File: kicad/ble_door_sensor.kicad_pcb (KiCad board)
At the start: 4 copper layers, 20 x 60 mm, 43 parts, among them J1 Prog Header, J2 Prog Header, P10 TestPoint, P12 TestPoint, P14 TestPoint, P19 TestPoint, P20 TestPoint, P27 TestPoint, P29 TestPoint, P3 TestPoint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

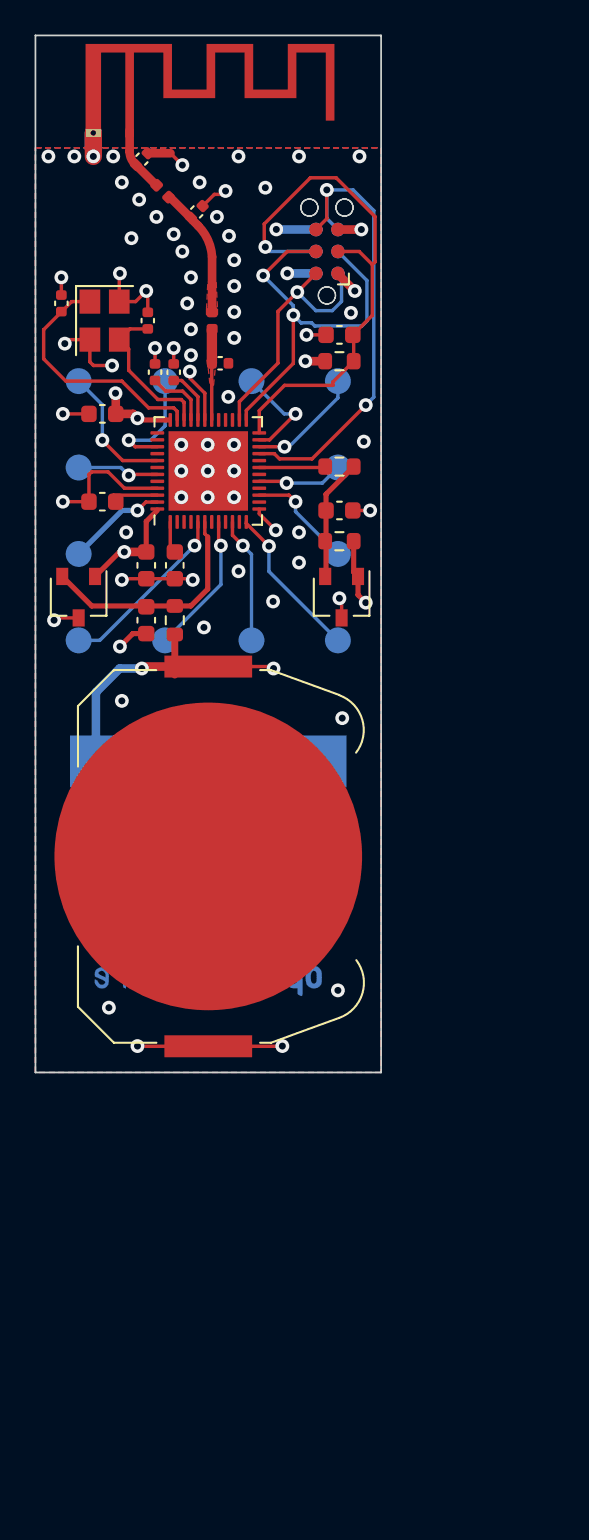
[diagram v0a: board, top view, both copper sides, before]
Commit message: First rough placement
Updated some footprints in the process to better fit my needs

Holes are in 5mm grid to each other 15mm in x and 45 mm in y apart

Board outline is 20x80mm
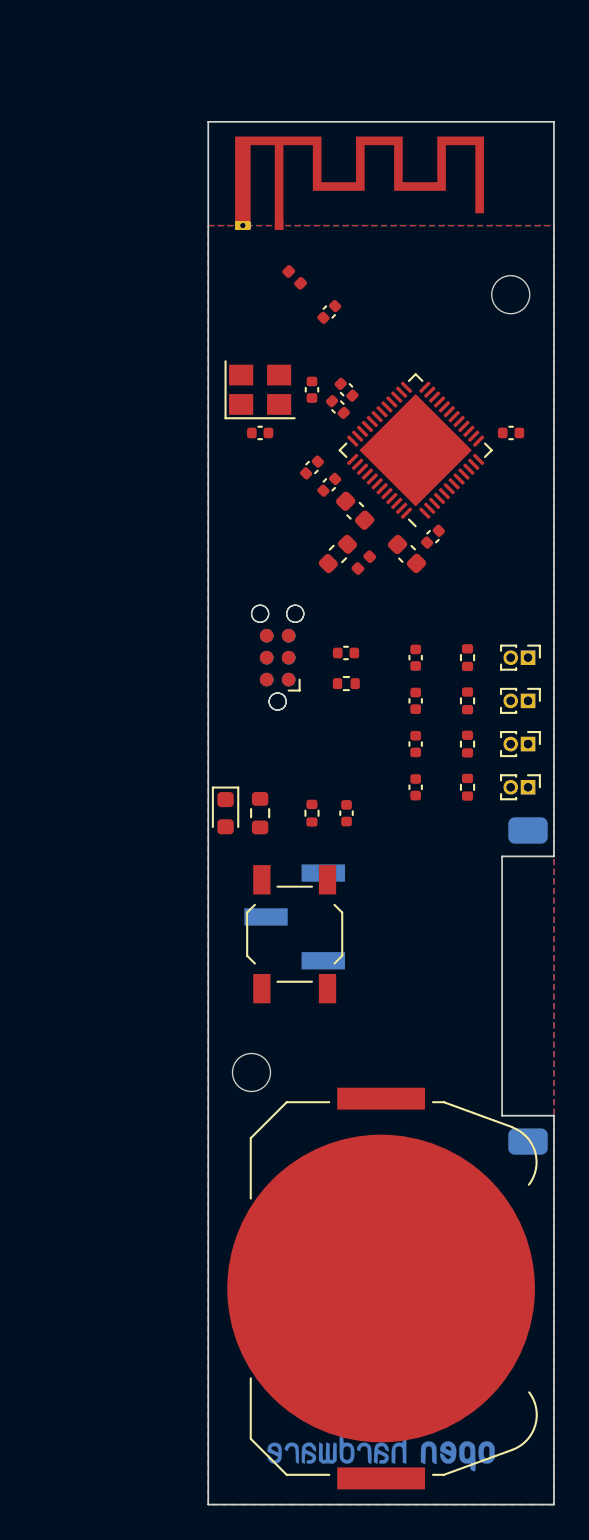
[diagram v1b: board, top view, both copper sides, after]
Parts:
- removed C10, C12: C_Small, Capacitor_SMD:C_0402_1005Metric
- removed C14: 100nF, Capacitor_SMD:C_0603_1608Metric
- removed DCC1, P10, P12, P14, P19, P20, P27, P29, P3, P31, P6, P8: TestPoint, TestPoint:TestPoint_Pad_D1.5mm
- removed L2: L, Inductor_SMD:L_0402_1005Metric
- removed R3: 0R, Resistor_SMD:R_0603_1608Metric
- removed R4: 470k, Resistor_SMD:R_0603_1608Metric
- removed U2, U3: A3214ELHLT-T, Package_TO_SOT_SMD:SOT-23W
- added C101: 100nF, Capacitor_SMD:C_0402_1005Metric, F.Cu at (133.0, 80.0)
- added C102: 100nF, Capacitor_SMD:C_0402_1005Metric, F.Cu at (137.0, 76.0)
- added C103: 100nF, Capacitor_SMD:C_0402_1005Metric, F.Cu at (137.0, 73.5)
- added C104: 100nF, Capacitor_SMD:C_0402_1005Metric, F.Cu at (137.0, 71.0)
- added C105: 12pF, Capacitor_SMD:C_0402_1005Metric, F.Cu at (132.0, 61.0)
- added C106: 12pF, Capacitor_SMD:C_0402_1005Metric, F.Cu at (131.0, 60.0)
- added D101: LED, LED_SMD:LED_0603_1608Metric, F.Cu at (126.0, 80.0)
- added H101: MountingHole, MountingHole:MountingHole_2.2mm_M2, F.Cu at (127.5, 95.0)
- added H102: MountingHole, MountingHole:MountingHole_2.2mm_M2, F.Cu at (142.5, 50.0)
- added J101: Conn_01x03_Pin, Connector_PinHeader_2.54mm:PinHeader_1x03_P2.54mm_Vertical_SMD_Pin1Left, B.Cu at (130.0, 86.0)
- added L101: 15nH, Inductor_SMD:L_0402_1005Metric, F.Cu at (134.0, 65.5)
- added L102: 10uH, Inductor_SMD:L_0603_1608Metric, F.Cu at (132.5, 65.0)
- added R101: 100k, Resistor_SMD:R_0402_1005Metric, F.Cu at (131.0, 80.0)
- added R102: 1K, Resistor_SMD:R_0603_1608Metric, F.Cu at (128.0, 80.0)
- added R103: 470k, Resistor_SMD:R_0402_1005Metric, F.Cu at (140.0, 76.0)
- added R104: 470k, Resistor_SMD:R_0402_1005Metric, F.Cu at (140.0, 73.5)
- added R105: 470k, Resistor_SMD:R_0402_1005Metric, F.Cu at (140.0, 71.0)
- added SW101: SW_Reed, Library:reed_contact, B.Cu at (143.5, 90.0)
- added SW102: SW_Push, Button_Switch_SMD:SW_SPST_TL3342, F.Cu at (130.0, 87.0)
- added SW103: REED_EXT, Connector_PinHeader_1.00mm:PinHeader_1x02_P1.00mm_Vertical, F.Cu at (143.5, 76.0)
- added SW104: REED_EXT, Connector_PinHeader_1.00mm:PinHeader_1x02_P1.00mm_Vertical, F.Cu at (143.5, 73.5)
- added SW105: REED_EXT, Connector_PinHeader_1.00mm:PinHeader_1x02_P1.00mm_Vertical, F.Cu at (143.5, 71.0)
- added SW106: REED_EXT, Connector_PinHeader_1.00mm:PinHeader_1x02_P1.00mm_Vertical, F.Cu at (143.5, 78.5)
- C1, C11, C13, C3: footprint Capacitor_SMD:C_0603_1608Metric -> Capacitor_SMD:C_0402_1005Metric
- L1: value 3.3nF -> 3.3nH
- R1, R2: footprint Resistor_SMD:R_0603_1608Metric -> Resistor_SMD:R_0402_1005Metric
- moved TP1 29.3 mm to (130.0, 104.0)
- moved REF** 29.3 mm to (135.0, 112.5)
- moved TP2 28.3 mm to (140.0, 104.0)
- moved BT1 26.9 mm to (135.0, 107.5)
- moved C1 23.7 mm to (142.5, 58.0), turned to 0 degrees
- moved J1 23.7 mm to (129.0, 71.0)
- moved J2 23.7 mm to (129.0, 71.0)
- moved R1 18.7 mm to (133.0, 72.5)
- moved C3 18.4 mm to (133.0, 70.7)
- moved C13 16.6 mm to (137.0, 78.5), turned to -90 degrees
- moved R2 16.1 mm to (140.0, 78.5), turned to 90 degrees
- moved C2 15.1 mm to (136.5, 65.0), turned to -45 degrees
- moved C11 15.0 mm to (138.0, 64.0), turned to -135 degrees
- moved C5 14.6 mm to (133.5, 62.5), turned to 135 degrees
- moved C6 13.7 mm to (128.0, 58.0), turned to 0 degrees
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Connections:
- C13 pad 1: Net-(U2-VOUT) -> ONBOARD_HALL
- L1 pad 2: Net-(C10-Pad1) -> Net-(AE1-A)
- R2 pad 2: Net-(U2-VOUT) -> ONBOARD_HALL
- U1 pad 10: Net-(U1-P0.08) -> unconnected-(U1-P0.08-Pad10)
- U1 pad 12: Net-(U1-NFC2/P0.10) -> unconnected-(U1-NFC2/P0.10-Pad12)
- U1 pad 14: unconnected-(U1-P0.11-Pad14) -> ONBOARD_HALL
- U1 pad 15: Net-(U1-P0.12) -> unconnected-(U1-P0.12-Pad15)
- U1 pad 17: Net-(U1-P0.14) -> unconnected-(U1-P0.14-Pad17)
- U1 pad 19: ONBOARD_HALL -> unconnected-(U1-P0.16-Pad19)
- U1 pad 22: Net-(U1-P0.19) -> unconnected-(U1-P0.19-Pad22)
- U1 pad 23: Net-(U1-P0.20) -> unconnected-(U1-P0.20-Pad23)
- U1 pad 37: unconnected-(U1-P0.25-Pad37) -> Net-(U1-P0.25)
- U1 pad 38: unconnected-(U1-P0.26-Pad38) -> Net-(U1-P0.26)
- U1 pad 39: Net-(U1-P0.27) -> unconnected-(U1-P0.27-Pad39)
- U1 pad 41: Net-(U1-P0.29/AIN5) -> unconnected-(U1-P0.29/AIN5-Pad41)
- U1 pad 43: Net-(U1-P0.31/AIN7) -> unconnected-(U1-P0.31/AIN7-Pad43)
- U1 pad 5: Net-(U1-P0.03/AIN1) -> unconnected-(U1-P0.03/AIN1-Pad5)
- U1 pad 6: ONBOARD_HALL_2 -> unconnected-(U1-P0.04/AIN2-Pad6)
- U1 pad 8: Net-(U1-P0.06) -> unconnected-(U1-P0.06-Pad8)
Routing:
- net VCC: track 46.3 -> 0.00 mm, vias 12 -> 0
- net GND: track 44.6 -> 0.00 mm, vias 68 -> 0
- net RESET: track 32.1 -> 0.00 mm, vias 1 -> 0
- net SWO: track 27.3 -> 0.00 mm, vias 2 -> 0
- net SWCLK: track 23.2 -> 0.00 mm, vias 2 -> 0
- net SWDIO: track 15.2 -> 0.00 mm, vias 1 -> 0
- net Net-(U1-XC2): track 14.5 -> 0.00 mm
- net ONBOARD_HALL_2: track 13.5 -> 0.00 mm
- net Net-(U1-P0.03/AIN1): track 10.4 -> 0.00 mm, vias 1 -> 0
- net Net-(U1-NFC2/P0.10): track 9.05 -> 0.00 mm, vias 1 -> 0
- net Net-(U1-XC1): track 8.90 -> 0.00 mm
- net Net-(U1-P0.06): track 8.24 -> 0.00 mm, vias 1 -> 0
- net Net-(U1-P0.29/AIN5): track 7.65 -> 0.00 mm, vias 1 -> 0
- net Net-(U1-P0.08): track 7.31 -> 0.00 mm, vias 1 -> 0
- net Net-(C10-Pad1): track 7.08 -> 0.00 mm
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- removed copper zone on F.Cu, net ANTENNA
- removed copper zone on F.Cu, net Net-(C10-Pad1)
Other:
- board size 20 x 60 mm -> 20 x 80 mm
- board text added: "EXT 1"
- board text added: "EXT 2"
- board text added: "EXT 3"
- board text added: "INT"
- board text added: "RX"
- board text added: "TX"
- board text added: "v0.2"
- board text removed: "DCC"
- board text removed: "v0.1"

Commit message: First routing
Replaced Testpoints with SMD pinheader
Added more Testpoints
Reduced board outline to 20x70mm
Mounting holes are now 15x35mm apart
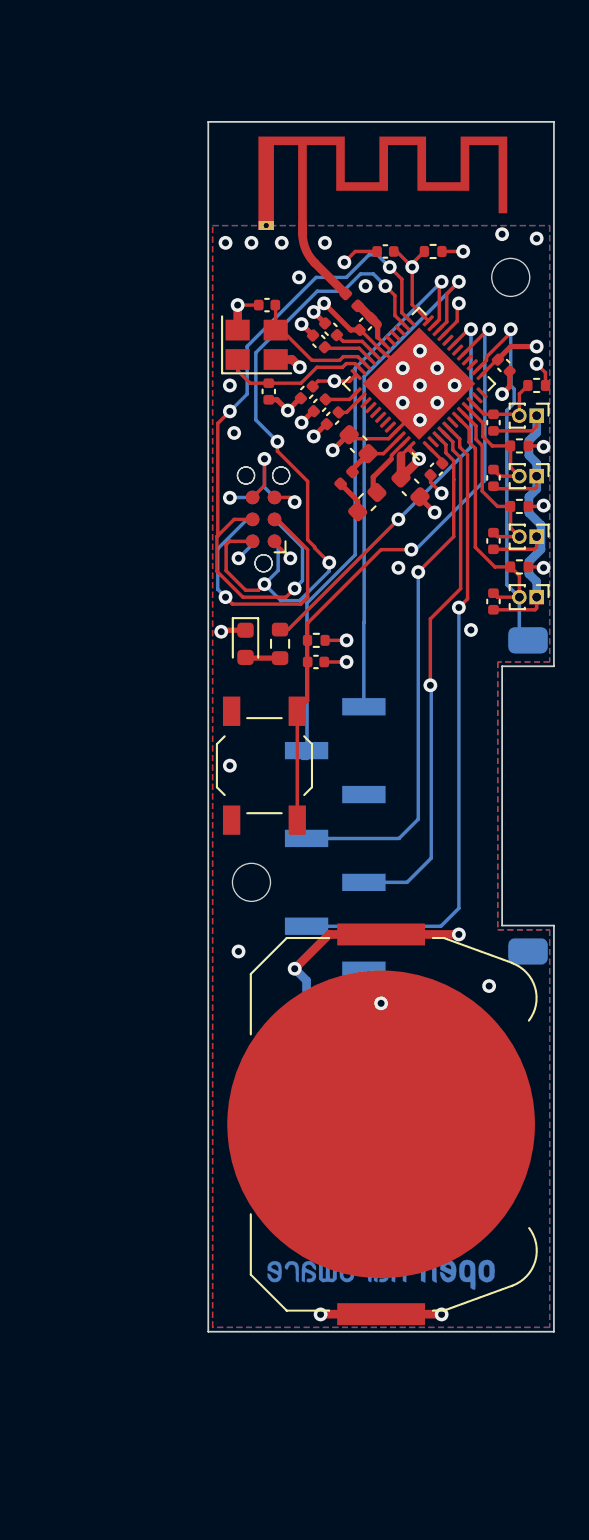
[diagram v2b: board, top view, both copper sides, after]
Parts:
- removed TP1, TP2: TestPoint, TestPoint:TestPoint_Pad_3.0x3.0mm
- added C107: 100nF, Capacitor_SMD:C_0402_1005Metric, F.Cu at (130.7, 55.6)
- J101: value Conn_01x03_Pin -> Conn_01x08; footprint Connector_PinHeader_2.54mm:PinHeader_1x03_P2.54mm_Vertical_SMD_Pin1Left -> Connector_PinHeader_2.54mm:PinHeader_1x08_P2.54mm_Vertical_SMD_Pin1Left
- moved R1 25.5 mm to (138.0, 47.5), turned to 180 degrees
- moved C3 23.3 mm to (135.2, 47.5)
- moved R105 16.3 mm to (144.0, 55.2), turned to 180 degrees
- moved R104 15.1 mm to (143.0, 58.8), turned to 180 degrees
- moved C104 14.3 mm to (141.5, 57.4)
- moved R103 14.1 mm to (143.0, 62.2), turned to 180 degrees
- moved SW105 14.0 mm to (144.0, 57.0)
- moved C103 13.7 mm to (141.5, 60.6)
- moved R2 13.1 mm to (143.0, 65.8), turned to 180 degrees
- moved SW104 13.0 mm to (144.0, 60.5)
- moved C102 12.6 mm to (141.5, 64.2)
- moved SW103 12.0 mm to (144.0, 64.0)
- moved C13 11.7 mm to (141.5, 67.8)
- moved SW106 11.0 mm to (144.0, 67.5)
- moved H101 11.0 mm to (127.5, 84.0)
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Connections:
- L101 pad 1: Net-(L101-Pad1) -> Net-(U1-DEC4)
- L101 pad 2: Net-(U1-DCC) -> Net-(L101-Pad2)
- L102 pad 1: Net-(U1-DEC4) -> Net-(L101-Pad2)
- L102 pad 2: Net-(L101-Pad1) -> Net-(U1-DCC)
- U1 pad 10: unconnected-(U1-P0.08-Pad10) -> EXT_HALL_3
- U1 pad 17: unconnected-(U1-P0.14-Pad17) -> BUTTON
- U1 pad 19: unconnected-(U1-P0.16-Pad19) -> LED
- U1 pad 22: unconnected-(U1-P0.19-Pad22) -> RX
- U1 pad 23: unconnected-(U1-P0.20-Pad23) -> TX
- U1 pad 3: unconnected-(U1-P0.01/XL2-Pad3) -> P0.01
- U1 pad 4: unconnected-(U1-P0.02/AIN0-Pad4) -> P0.02
- U1 pad 5: unconnected-(U1-P0.03/AIN1-Pad5) -> P0.03
- U1 pad 7: unconnected-(U1-P0.05/AIN3-Pad7) -> ONBOARD_HALL
- U1 pad 8: unconnected-(U1-P0.06-Pad8) -> EXT_HALL_1
- U1 pad 9: unconnected-(U1-P0.07-Pad9) -> EXT_HALL_2
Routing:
- net GND: track 0.00 -> 73.1 mm, vias 0 -> 42
- net RESET: track 0.00 -> 49.3 mm, vias 0 -> 2
- net VCC: track 0.00 -> 40.9 mm, vias 0 -> 15
- net SWCLK: track 0.00 -> 40.7 mm, vias 0 -> 3
- net SWDIO: track 0.00 -> 40.5 mm, vias 0 -> 4
- net P0.03: track 0.00 -> 37.8 mm, vias 0 -> 1
- net BUTTON: track 0.00 -> 36.3 mm, vias 0 -> 2
- net ONBOARD_HALL: track 0.00 -> 35.9 mm, vias 0 -> 1
- net TX: track 0.00 -> 34.1 mm, vias 0 -> 1
- net P0.02: track 0.00 -> 30.7 mm, vias 0 -> 1
- net P0.01: track 0.00 -> 30.3 mm, vias 0 -> 1
- net RX: track 0.00 -> 30.2 mm, vias 0 -> 1
- net SWO: track 0.00 -> 24.7 mm, vias 0 -> 2
- net LED: track 0.00 -> 23.7 mm, vias 0 -> 2
- net EXT_HALL_1: track 0.00 -> 10.6 mm
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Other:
- board size 20 x 80 mm -> 20 x 70 mm
- board text added: "Door Monitor v0.2"
- board text added: "Fabian Pflug"
- board text added: "P0.01"
- board text added: "P0.02"
- board text added: "P0.03"
- board text removed: "Door Monitor"
- board text removed: "v0.2"

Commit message: Put the reed contact on the top side
I want to glue the PCB to some surfaces and having something on the
bottom side is very contraproductive.
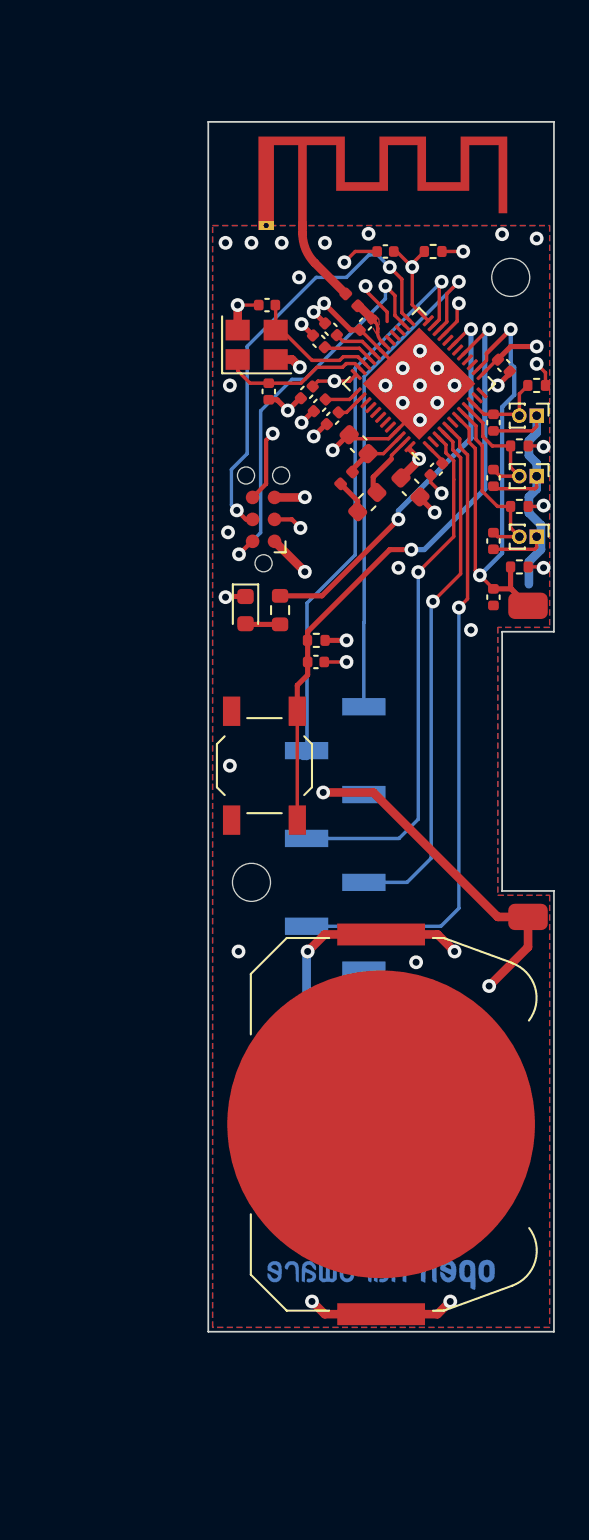
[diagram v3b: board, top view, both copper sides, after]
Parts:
- removed J2: Prog Header, Connector:Tag-Connect_TC2030-IDC-NL_2x03_P1.27mm_Vertical
- removed SW106: REED_EXT, Connector_PinHeader_1.00mm:PinHeader_1x02_P1.00mm_Vertical
- C102, C103, C104, C13: value 100nF -> 10nF
- R103, R104, R105, R2: value 470k -> 1M
- SW101: moved to F.Cu
- moved SW101 2.00 mm to (143.5, 77.0)
- moved D101 1.95 mm to (127.2, 68.2)
- moved R102 1.95 mm to (129.2, 68.2)
- moved C13 0.25 mm to (141.5, 67.5)
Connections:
- SW101 pad 1: GND -> ONBOARD_HALL
- SW101 pad 2: ONBOARD_HALL -> GND
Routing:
- net RESET: track 49.3 -> 30.9 mm
- net SWDIO: track 40.5 -> 23.3 mm, vias 4 -> 2
- net GND: track 73.1 -> 88.6 mm, vias 42 -> 43
- net SWCLK: track 40.7 -> 25.4 mm, vias 3 -> 2
- net SWO: track 24.7 -> 22.3 mm
- net ONBOARD_HALL: track 35.9 -> 34.1 mm, vias 1 -> 2
- net VCC: track 40.9 -> 40.0 mm, vias 15 -> 14
- net LED: track 23.7 -> 22.9 mm
- added copper zone on F.Cu, net ANTENNA
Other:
- outline, holes or cut-outs redrawn
- board text removed: "INT"

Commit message: Add Temperature sensor instead of external reed
Remove the contacts fro external reed contacts
Add temperature sensor
Reduce the size of the PCB
Add additional mounting hole
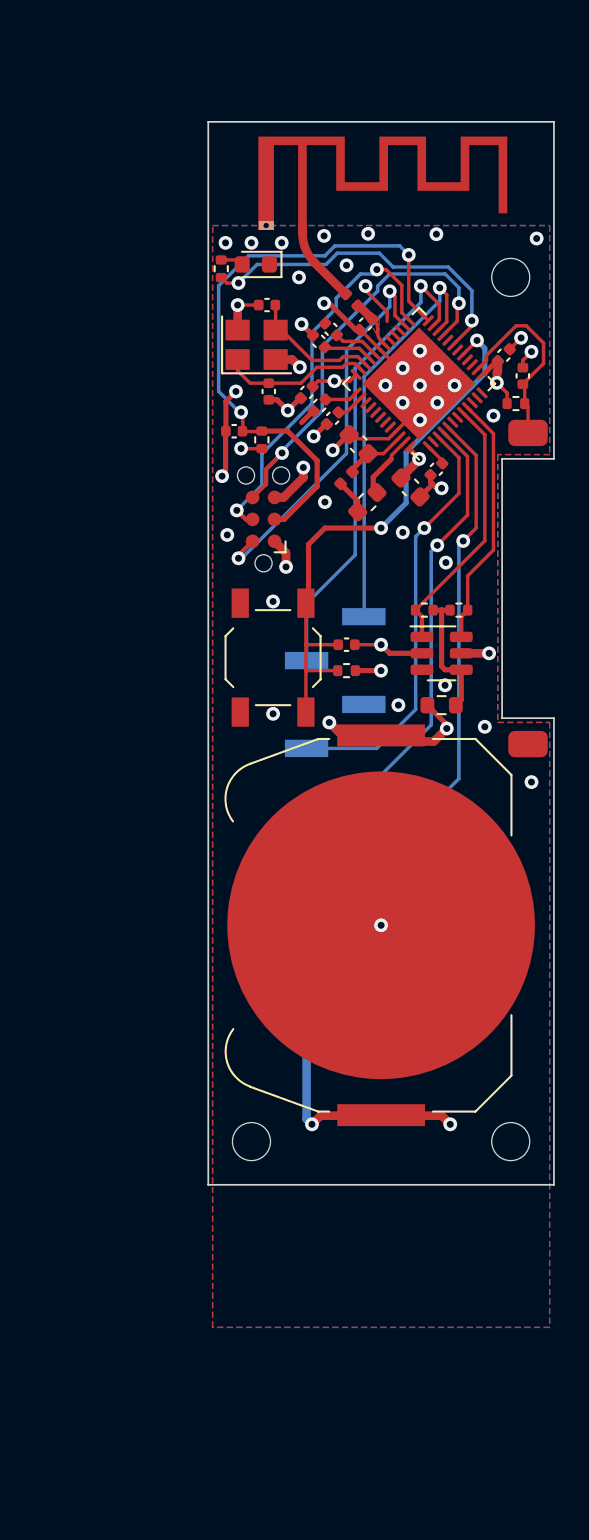
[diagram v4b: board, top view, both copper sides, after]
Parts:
- removed C102, C103, C104: 10nF, Capacitor_SMD:C_0402_1005Metric
- removed REF**: OSHW-Logo2_14.6x12mm_Copper, Symbol:OSHW-Logo2_14.6x12mm_Copper
- removed SW103, SW104, SW105: REED_EXT, Connector_PinHeader_1.00mm:PinHeader_1x02_P1.00mm_Vertical
- added H103: MountingHole, MountingHole:MountingHole_2.2mm_M2, F.Cu at (142.5, 99.0)
- added U101: TMP100, Package_TO_SOT_SMD:SOT-23-6, F.Cu at (138.5, 70.8)
- R102: footprint Resistor_SMD:R_0603_1608Metric -> Resistor_SMD:R_0402_1005Metric
- R103: value 1M -> 0; footprint Resistor_SMD:R_0402_1005Metric -> Resistor_SMD:R_0603_1608Metric
- R104, R105: value 1M -> 100k
- moved R102 20.0 mm to (125.8, 48.5), turned to 90 degrees
- moved D101 20.0 mm to (127.8, 48.2), turned to 180 degrees
- moved H101 15.0 mm to (127.5, 99.0)
- moved R1 14.7 mm to (128.1, 58.4), turned to 90 degrees
- moved R105 14.5 mm to (137.5, 68.2)
- moved C3 13.6 mm to (126.5, 57.9)
- moved C13 12.9 mm to (143.2, 54.7), turned to 90 degrees
- moved R103 12.3 mm to (138.5, 73.8), turned to 0 degrees
- moved BT1 11.5 mm to (135.0, 86.5), turned to -90 degrees
- moved R104 10.1 mm to (139.5, 68.2), turned to 0 degrees
- moved SW101 10.0 mm to (143.5, 67.0)
- moved R2 9.45 mm to (142.8, 56.3), turned to 0 degrees
- moved SW102 6.27 mm to (128.8, 71.0)
- moved J101 5.21 mm to (132.3, 77.5)
- moved R101 2.47 mm to (133.0, 71.8)
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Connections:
- net EXT_HALL_2 renamed SDA
- net Net-(AE1-A) renamed /Antenne
- net Net-(U1-DEC1) renamed /DEC1
- net Net-(U1-DEC2) renamed /DEC2
- net Net-(U1-DEC3) renamed /DEC3
- net Net-(U1-DEC4) renamed /DEC4
- net Net-(U1-XC1) renamed /XC1
- net Net-(U1-XC2) renamed /XC2
- R103 pad 2: EXT_HALL_1 -> /VCC_Temp
- R104 pad 1: VCC -> /VCC_Temp
- R105 pad 1: VCC -> /VCC_Temp
- R105 pad 2: EXT_HALL_3 -> SCL
- U1 pad 10: EXT_HALL_3 -> unconnected-(U1-P0.08-Pad10)
- U1 pad 7: ONBOARD_HALL -> unconnected-(U1-P0.05/AIN3-Pad7)
- U1 pad 8: EXT_HALL_1 -> SCL
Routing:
- net ONBOARD_HALL: track 34.1 -> 11.3 mm, vias 2 -> 0
- net GND: track 88.6 -> 66.2 mm, vias 43 -> 46
- net SCL: track 0.00 -> 15.3 mm
- net EXT_HALL_1: track 10.6 -> 0.00 mm
- net /VCC_Temp: track 0.00 -> 7.63 mm
- net SDA: track 7.49 -> 14.7 mm
- net TX: track 34.1 -> 27.3 mm
- net RX: track 30.2 -> 23.7 mm
- net P0.02: track 30.7 -> 24.4 mm
- net P0.03: track 37.8 -> 31.6 mm
- net P0.01: track 30.3 -> 24.6 mm
- net EXT_HALL_3: track 4.99 -> 0.00 mm
- net RESET: track 30.9 -> 35.3 mm
- net BUTTON: track 36.3 -> 32.8 mm
- net VCC: track 40.0 -> 43.2 mm, vias 14 -> 10
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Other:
- board size 20 x 70 mm -> 20 x 61.5 mm
- board text added: "https://gumulka.eu/ble_door_sensor"
- board text removed: "EXT 1"
- board text removed: "EXT 2"
- board text removed: "EXT 3"
